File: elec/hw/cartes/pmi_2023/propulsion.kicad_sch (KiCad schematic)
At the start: 45 parts, among them Q1 SI2310, U1 DRV8231ADDAR, U2 DRV8231ADDAR, U3 EESX1321, U4 EESX1321

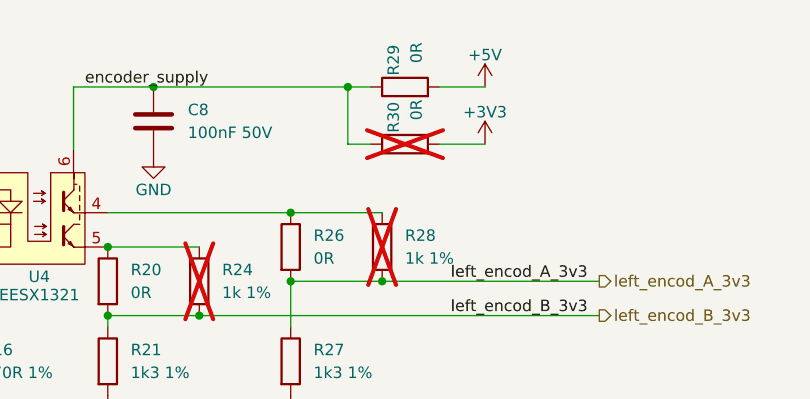
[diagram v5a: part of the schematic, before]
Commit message: modified mounting hole, replaced transistors to place them in bottom layer
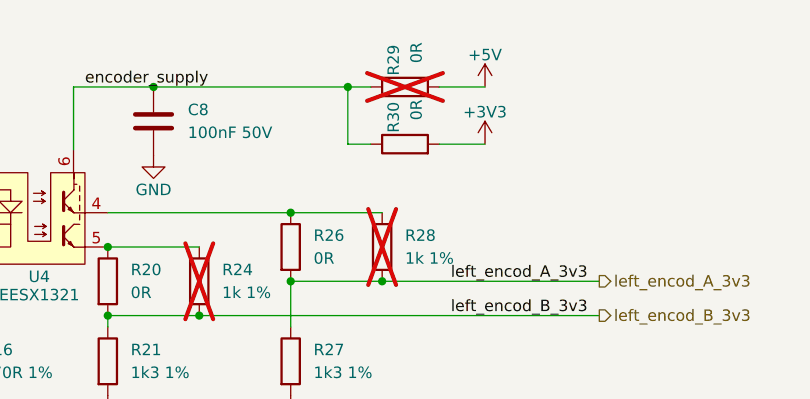
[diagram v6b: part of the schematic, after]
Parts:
- R29: now not fitted
- R30: now fitted
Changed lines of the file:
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@@
 		(in_bom yes)
 		(on_board yes)
-		(dnp yes)
+		(dnp no)
 		(property "Reference" "R30"
 			(at 207.01 35.56 0)
@@
 		(in_bom yes)
 		(on_board yes)
-		(dnp no)
+		(dnp yes)
 		(property "Reference" "R29"
 			(at 207.01 29.21 0)

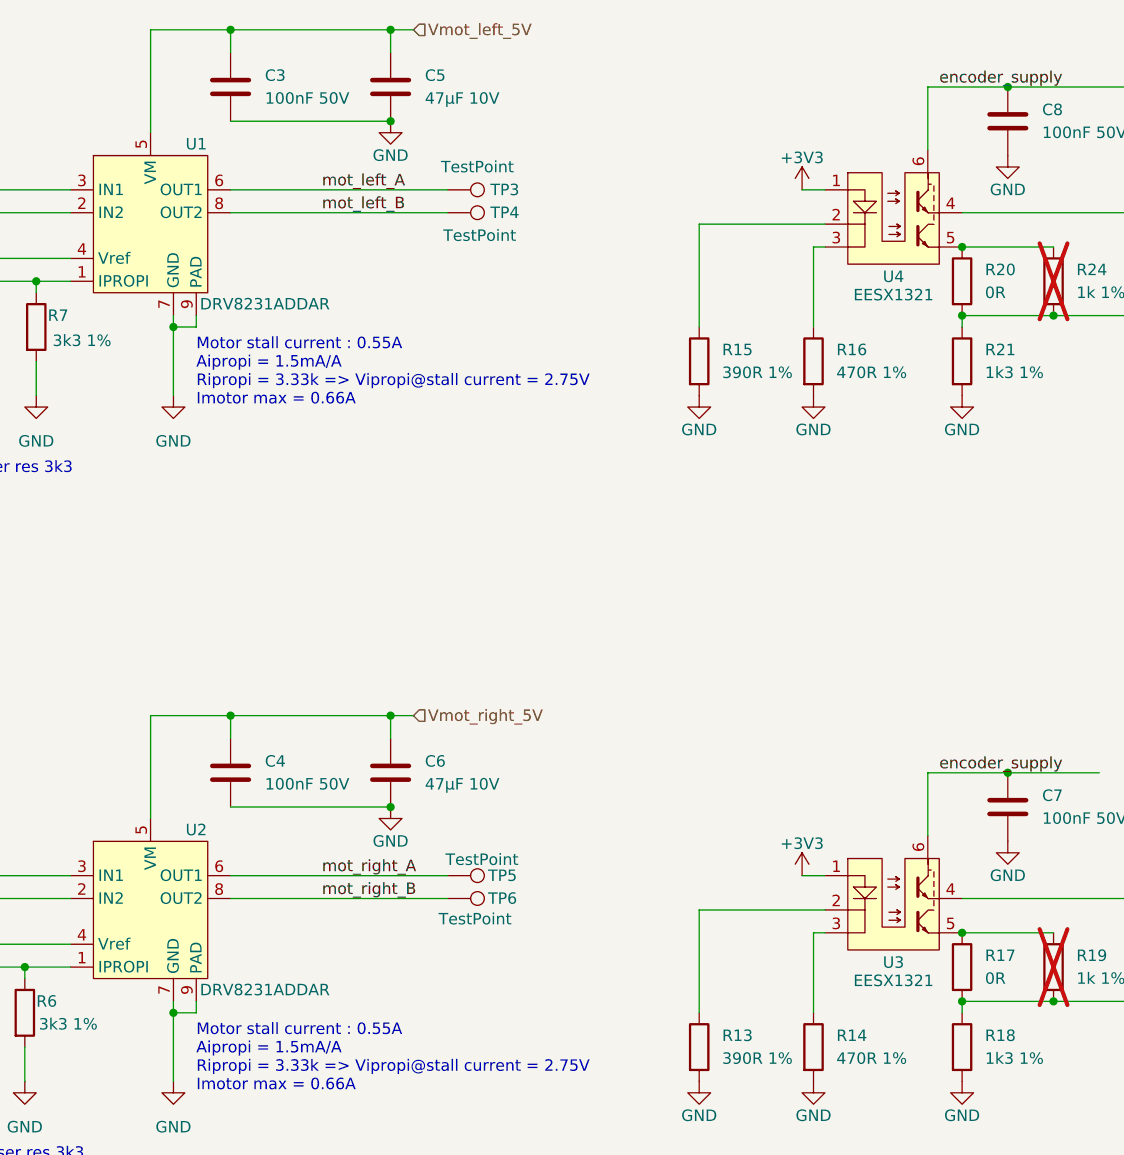
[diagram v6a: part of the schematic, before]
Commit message: XRA1200 replaced by TCA6408
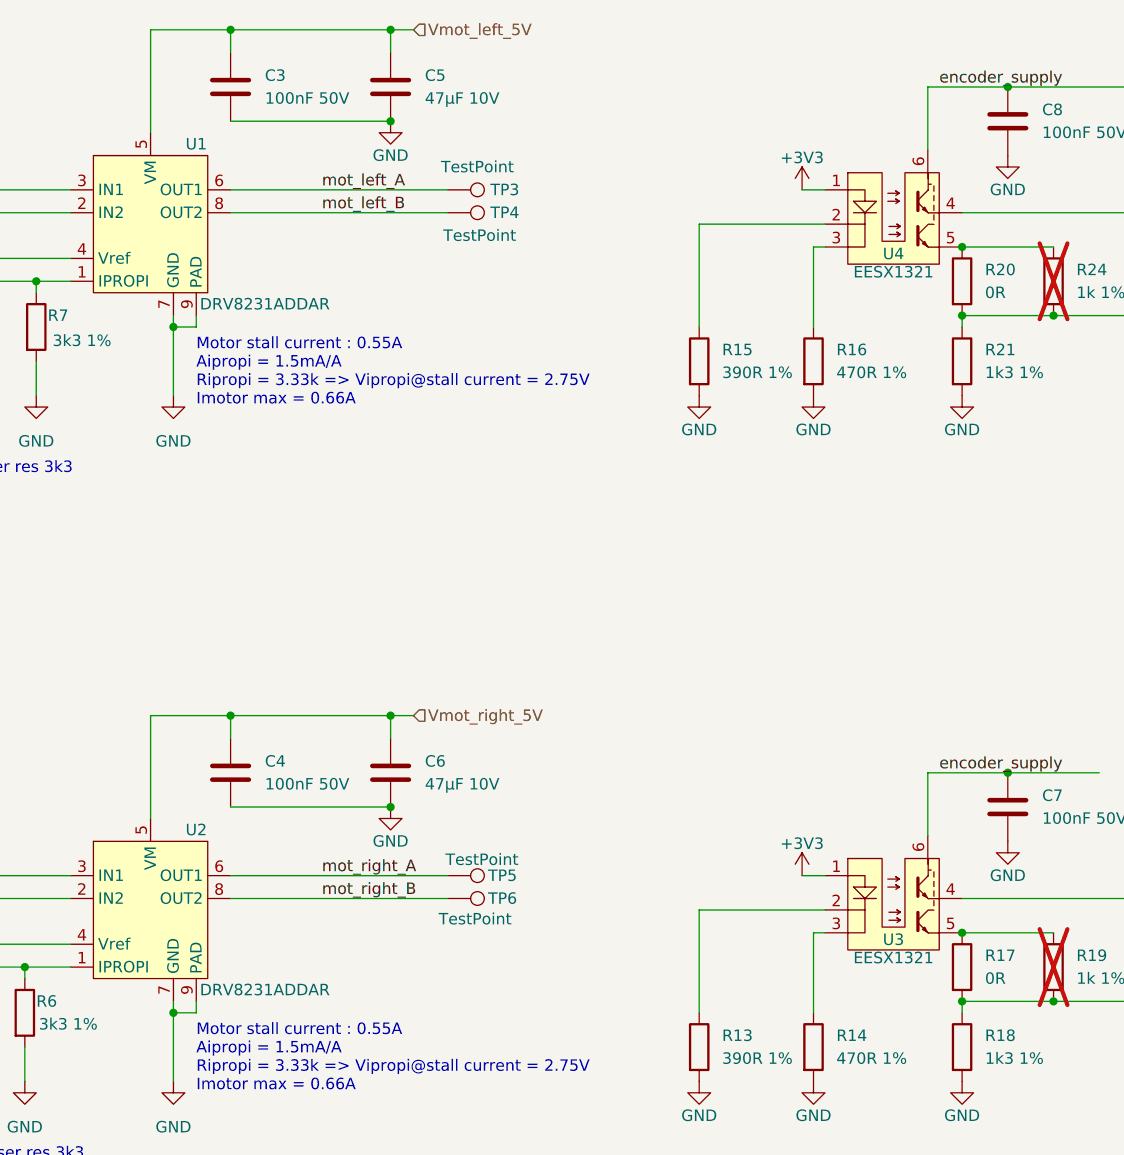
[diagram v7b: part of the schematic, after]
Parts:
- C1, C2, C3, C4, C7, C8: JLCPCB C14663 -> (none); JLCPCB Part # (none) -> C14663
- C5, C6: JLCPCB C96123 -> (none); JLCPCB Part # (none) -> C96123
- Q1: JLCPCB C2938374 -> (none); JLCPCB Part # (none) -> C2938374
- R1, R2, R3, R4, R5: JLCPCB C25803 -> (none); JLCPCB Part # (none) -> C25803
- R13, R15: JLCPCB C23151 -> (none); JLCPCB Part # (none) -> C23151
- R14, R16: JLCPCB C23179 -> (none); JLCPCB Part # (none) -> C23179
- R17, R20, R22, R26, R29, R30, R8: JLCPCB C431718 -> (none); JLCPCB Part # (none) -> C431718
- R18, R21, R23, R27: JLCPCB C22767 -> (none); JLCPCB Part # (none) -> C22767
- R19, R24, R25, R28: JLCPCB C21190 -> (none); JLCPCB Part # (none) -> C2991540
- R6, R7: JLCPCB C22978 -> (none); JLCPCB Part # (none) -> C22978
- U1, U2: JLCPCB C5218849 -> (none); JLCPCB Part # (none) -> C5218849
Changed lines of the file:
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@@
 	(paper "A4")
 	(junction
+		(at 175.26 48.26)
+		(diameter 0)
+		(color 0 0 0 0)
+	)
+	(junction
 		(at 175.26 55.88)
 		(diameter 0)
@@
 	)
 	(junction
+		(at 175.26 124.46)
+		(diameter 0)
+		(color 0 0 0 0)
+	)
+	(junction
 		(at 201.93 30.48)
 		(diameter 0)
@@
 		(color 0 0 0 0)
 	)
-	(junction
-		(at 175.26 48.26)
-		(diameter 0)
-		(color 0 0 0 0)
-	)
-	(junction
-		(at 175.26 124.46)
-		(diameter 0)
-		(color 0 0 0 0)
-	)
 	(wire
 		(pts
@@
 	(wire
 		(pts
-			(xy 160.02 48.26) (xy 158.75 48.26)
-		)
-		(stroke
-			(width 0)
-			(type default)
-		)
-	)
-	(wire
-		(pts
 			(xy 87.63 133.35) (xy 87.63 132.08)
 		)
@@
 	(wire
 		(pts
-			(xy 160.02 124.46) (xy 158.75 124.46)
+			(xy 157.48 118.11) (xy 160.02 118.11)
 		)
 		(stroke
@@
 	(wire
 		(pts
-			(xy 157.48 118.11) (xy 160.02 118.11)
+			(xy 158.75 124.46) (xy 158.75 133.35)
 		)
 		(stroke
@@
 	(wire
 		(pts
-			(xy 158.75 124.46) (xy 158.75 133.35)
+			(xy 45.72 49.53) (xy 45.72 54.61)
 		)
 		(stroke
@@
 	(wire
 		(pts
-			(xy 45.72 49.53) (xy 45.72 54.61)
+			(xy 85.09 100.33) (xy 93.98 100.33)
 		)
 		(stroke
@@
 	(wire
 		(pts
-			(xy 85.09 100.33) (xy 93.98 100.33)
+			(xy 45.72 140.97) (xy 45.72 138.43)
 		)
 		(stroke
@@
 	(wire
 		(pts
-			(xy 45.72 140.97) (xy 45.72 138.43)
+			(xy 217.17 36.83) (xy 212.09 36.83)
 		)
 		(stroke
@@
 	(wire
 		(pts
-			(xy 217.17 36.83) (xy 212.09 36.83)
+			(xy 180.34 30.48) (xy 201.93 30.48)
 		)
 		(stroke
@@
 	(wire
 		(pts
-			(xy 180.34 30.48) (xy 201.93 30.48)
+			(xy 158.75 48.26) (xy 160.02 48.26)
 		)
 		(stroke
@@
 	(wire
 		(pts
+			(xy 158.75 124.46) (xy 160.02 124.46)
+		)
+		(stroke
+			(width 0)
+			(type default)
+		)
+	)
+	(wire
+		(pts
 			(xy 45.72 64.77) (xy 45.72 62.23)
 		)
@@
 			)
 		)
-		(property "JLCPCB" "C23179"
+		(property "JLCPCB Part #" "C23179"
 			(at 158.75 137.16 0)
 			(effects
@@
 			)
 		)
-		(property "JLCPCB" "C14663"
+		(property "JLCPCB Part #" "C14663"
 			(at 45.72 58.42 0)
 			(effects
@@
 			)
 		)
-		(property "JLCPCB" "C21190"
+		(property "JLCPCB Part #" "C2991540"
 			(at 205.74 124.46 0)
 			(effects
@@
 			)
 		)
-		(property "JLCPCB" "C431718"
+		(property "JLCPCB Part #" "C431718"
 			(at 175.26 128.27 0)
 			(effects
@@
 			)
 		)
-		(property "JLCPCB" "C21190"
+		(property "JLCPCB Part #" "C2991540"
 			(at 185.42 128.27 0)
 			(effects
@@
 			)
 		)
-		(property "JLCPCB" "C25803"
+		(property "JLCPCB Part #" "C25803"
 			(at 52.07 184.15 0)
 			(effects
@@
 			)
 		)
-		(property "JLCPCB" "C431718"
+		(property "JLCPCB Part #" "C431718"
 			(at 195.58 48.26 0)
 			(effects
@@
 			)
 		)
-		(property "JLCPCB" "C14663"
+		(property "JLCPCB Part #" "C14663"
 			(at 93.98 30.48 0)
 			(effects
@@
 			)
 		)
-		(property "JLCPCB" "C2938374"
+		(property "JLCPCB Part #" "C2938374"
 			(at 83.82 177.8 0)
 			(effects
@@
 			)
 		)
-		(property "JLCPCB" "C431718"
+		(property "JLCPCB Part #" "C431718"
 			(at 175.26 52.07 0)
 			(effects
@@
 			)
 		)
-		(property "JLCPCB" "C25803"
+		(property "JLCPCB Part #" "C25803"
 			(at 26.67 132.08 0)
 			(effects
@@
 			)
 		)
-		(property "JLCPCB" "C431718"
+		(property "JLCPCB Part #" "C431718"
 			(at 80.01 166.37 0)
 			(effects
@@
 			)
 		)
-		(property "JLCPCB" "C5218849"
+		(property "JLCPCB Part #" "C5218849"
 			(at 85.09 46.99 0)
 			(effects
@@
 			)
 		)
-		(property "JLCPCB" "C14663"
+		(property "JLCPCB Part #" "C14663"
 			(at 45.72 134.62 0)
 			(effects
@@
 			)
 		)
-		(property "JLCPCB" "C21190"
+		(property "JLCPCB Part #" "C2991540"
 			(at 185.42 52.07 0)
 			(effects
@@
 	(symbol
 		(lib_id "cocotter_ic:EESX1321")
-		(at 167.64 121.92 0)
+		(at 167.64 119.38 0)
 		(unit 1)
 		(exclude_from_sim no)
@@
 		(dnp no)
 		(property "Reference" "U3"
-			(at 167.64 127.762 0)
+			(at 167.64 125.222 0)
 			(effects
 				(font
@@
 		)
 		(property "Value" "EESX1321"
-			(at 167.64 129.794 0)
+			(at 167.64 127.254 0)
 			(effects
 				(font
@@
 		)
 		(property "Footprint" "cocotter_ic:EESX1321"
-			(at 176.53 116.84 0)
+			(at 176.53 114.3 0)
 			(effects
 				(font
@@
 		)
 		(property "Datasheet" ""
-			(at 176.53 116.84 0)
+			(at 176.53 114.3 0)
 			(effects
 				(font
@@
 		)
 		(property "Description" ""
-			(at 167.64 121.92 0)
+			(at 167.64 119.38 0)
 			(effects
 				(font
@@
 			)
 		)
-		(property "JLCPCB" "C22767"
+		(property "JLCPCB Part #" "C22767"
 			(at 195.58 60.96 0)
 			(effects
@@
 			)
 		)
-		(property "JLCPCB" "C22767"
+		(property "JLCPCB Part #" "C22767"
 			(at 195.58 137.16 0)
 			(effects
@@
 			)
 		)
-		(property "JLCPCB" "C96123"
+		(property "JLCPCB Part #" "C96123"
 			(at 111.76 30.48 0)
 			(effects
@@
 			)
 		)
-		(property "JLCPCB" "C25803"
+		(property "JLCPCB Part #" "C25803"
 			(at 35.56 132.08 0)
 			(effects
@@
 			)
 		)
-		(property "JLCPCB" "C21190"
+		(property "JLCPCB Part #" "C2991540"
 			(at 205.74 48.26 0)
 			(effects
@@
 			)
 		)
-		(property "JLCPCB" "C5218849"
+		(property "JLCPCB Part #" "C5218849"
 			(at 85.09 123.19 0)
 			(effects
@@
 			)
 		)
-		(property "JLCPCB" "C431718"
+		(property "JLCPCB Part #" "C431718"
 			(at 208.28 36.83 0)
 			(effects
@@
 			)
 		)
-		(property "JLCPCB" "C14663"
+		(property "JLCPCB Part #" "C14663"
 			(at 180.34 34.29 0)
 			(effects
@@
 	(symbol
 		(lib_id "cocotter_ic:EESX1321")
-		(at 167.64 45.72 0)
+		(at 167.64 43.18 0)
 		(unit 1)
 		(exclude_from_sim no)
@@
 		(dnp no)
 		(property "Reference" "U4"
-			(at 167.64 51.562 0)
+			(at 167.64 49.022 0)
 			(effects
 				(font
@@
 		)
 		(property "Value" "EESX1321"
-			(at 167.64 53.594 0)
+			(at 167.64 51.054 0)
 			(effects
 				(font
@@
 		)
 		(property "Footprint" "cocotter_ic:EESX1321"
-			(at 176.53 40.64 0)
+			(at 176.53 38.1 0)
 			(effects
 				(font
@@
 		)
 		(property "Datasheet" ""
-			(at 176.53 40.64 0)
+			(at 176.53 38.1 0)
 			(effects
 				(font
@@
 		)
 		(property "Description" ""
-			(at 167.64 45.72 0)
+			(at 167.64 43.18 0)
 			(effects
 				(font
@@
 			)
 		)
-		(property "JLCPCB" "C22978"
+		(property "JLCPCB Part #" "C22978"
 			(at 71.12 133.35 0)
 			(effects
@@
 			)
 		)
-		(property "JLCPCB" "C23151"
+		(property "JLCPCB Part #" "C23151"
 			(at 146.05 137.16 0)
 			(effects
@@
 			)
 		)
-		(property "JLCPCB" "C431718"
+		(property "JLCPCB Part #" "C431718"
 			(at 195.58 124.46 0)
 			(effects
@@
 			)
 		)
-		(property "JLCPCB" "C14663"
+		(property "JLCPCB Part #" "C14663"
 			(at 180.34 110.49 0)
 			(effects
@@
 			)
 		)
-		(property "JLCPCB" "C23179"
+		(property "JLCPCB Part #" "C23179"
 			(at 158.75 60.96 0)
 			(effects
@@
 			)
 		)
-		(property "JLCPCB" "C96123"
+		(property "JLCPCB Part #" "C96123"
 			(at 111.76 106.68 0)
 			(effects
@@
 			)
 		)
-		(property "JLCPCB" "C14663"
+		(property "JLCPCB Part #" "C14663"
 			(at 93.98 106.68 0)
 			(effects
@@
 			)
 		)
-		(property "JLCPCB" "C25803"
+		(property "JLCPCB Part #" "C25803"
 			(at 26.67 55.88 0)
 			(effects
@@
 			)
 		)
-		(property "JLCPCB" "C22767"
+		(property "JLCPCB Part #" "C22767"
 			(at 175.26 137.16 0)
 			(effects
@@
 			)
 		)
-		(property "JLCPCB" "C22767"
+		(property "JLCPCB Part #" "C22767"
 			(at 175.26 60.96 0)
 			(effects
@@
 			)
 		)
-		(property "JLCPCB" "C22978"
+		(property "JLCPCB Part #" "C22978"
 			(at 72.39 57.15 0)
 			(effects
@@
 			)
 		)
-		(property "JLCPCB" "C23151"
+		(property "JLCPCB Part #" "C23151"
 			(at 146.05 60.96 0)
 			(effects
@@
 			)
 		)
-		(property "JLCPCB" "C25803"
+		(property "JLCPCB Part #" "C25803"
 			(at 35.56 55.88 0)
 			(effects
@@
 			)
 		)
-		(property "JLCPCB" "C431718"
+		(property "JLCPCB Part #" "C431718"
 			(at 208.28 30.48 0)
 			(effects

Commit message: bom updated and component selection optimized to decrease bom cost
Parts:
- R1, R2, R3, R4, R5: value 100k -> 91k 1%; symbol cocotter_resistors:R_100k_0603_1% -> cocotter_resistors:R_91k_0603_1%; JLCPCB Part # C25803 -> C23265; Specification 100k 0603 1% 100mW -> 91k 0603 1% 100mW; mouser 603-RC0603FR-10100KL -> (none)
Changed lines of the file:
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@@
 	)
 	(symbol
-		(lib_id "cocotter_resistors:R_100k_0603_1%")
+		(lib_id "cocotter_resistors:R_91k_0603_1%")
 		(at 52.07 184.15 0)
 		(unit 1)
@@
 			)
 		)
-		(property "Value" "100k"
+		(property "Value" "91k 1%"
 			(at 54.61 185.4199 0)
 			(effects
@@
 			)
 		)
-		(property "Specification" "100k 0603 1% 100mW"
+		(property "Specification" "91k 0603 1% 100mW"
 			(at 52.07 184.15 0)
 			(effects
@@
 			)
 		)
-		(property "mouser" "603-RC0603FR-10100KL"
+		(property "mouser" ""
 			(at 52.07 184.15 0)
 			(effects
@@
 			)
 		)
-		(property "JLCPCB Part #" "C25803"
+		(property "JLCPCB Part #" "C23265"
 			(at 52.07 184.15 0)
 			(effects
@@
 	)
 	(symbol
-		(lib_id "cocotter_resistors:R_100k_0603_1%")
+		(lib_id "cocotter_resistors:R_91k_0603_1%")
 		(at 26.67 132.08 0)
 		(unit 1)
@@
 			)
 		)
-		(property "Value" "100k"
+		(property "Value" "91k 1%"
 			(at 29.21 133.3499 0)
 			(effects
@@
 			)
 		)
-		(property "Specification" "100k 0603 1% 100mW"
+		(property "Specification" "91k 0603 1% 100mW"
 			(at 26.67 132.08 0)
 			(effects
@@
 			)
 		)
-		(property "mouser" "603-RC0603FR-10100KL"
+		(property "mouser" ""
 			(at 26.67 132.08 0)
 			(effects
@@
 			)
 		)
-		(property "JLCPCB Part #" "C25803"
+		(property "JLCPCB Part #" "C23265"
 			(at 26.67 132.08 0)
 			(effects
@@
 	)
 	(symbol
-		(lib_id "cocotter_resistors:R_100k_0603_1%")
+		(lib_id "cocotter_resistors:R_91k_0603_1%")
 		(at 35.56 132.08 0)
 		(unit 1)
@@
 			)
 		)
-		(property "Value" "100k"
+		(property "Value" "91k 1%"
 			(at 38.1 133.3499 0)
 			(effects
@@
 			)
 		)
-		(property "Specification" "100k 0603 1% 100mW"
+		(property "Specification" "91k 0603 1% 100mW"
 			(at 35.56 132.08 0)
 			(effects
@@
 			)
 		)
-		(property "mouser" "603-RC0603FR-10100KL"
+		(property "mouser" ""
 			(at 35.56 132.08 0)
 			(effects
@@
 			)
 		)
-		(property "JLCPCB Part #" "C25803"
+		(property "JLCPCB Part #" "C23265"
 			(at 35.56 132.08 0)
 			(effects
@@
 	)
 	(symbol
-		(lib_id "cocotter_resistors:R_100k_0603_1%")
+		(lib_id "cocotter_resistors:R_91k_0603_1%")
 		(at 26.67 55.88 0)
 		(unit 1)
@@
 			)
 		)
-		(property "Value" "100k"
+		(property "Value" "91k 1%"
 			(at 29.21 57.1499 0)
 			(effects
@@
 			)
 		)
-		(property "Specification" "100k 0603 1% 100mW"
+		(property "Specification" "91k 0603 1% 100mW"
 			(at 26.67 55.88 0)
 			(effects
@@
 			)
 		)
-		(property "mouser" "603-RC0603FR-10100KL"
+		(property "mouser" ""
 			(at 26.67 55.88 0)
 			(effects
@@
 			)
 		)
-		(property "JLCPCB Part #" "C25803"
+		(property "JLCPCB Part #" "C23265"
 			(at 26.67 55.88 0)
 			(effects
@@
 	)
 	(symbol
-		(lib_id "cocotter_resistors:R_100k_0603_1%")
+		(lib_id "cocotter_resistors:R_91k_0603_1%")
 		(at 35.56 55.88 0)
 		(unit 1)
@@
 			)
 		)
-		(property "Value" "100k"
+		(property "Value" "91k 1%"
 			(at 38.1 57.1499 0)
 			(effects
@@
 			)
 		)
-		(property "Specification" "100k 0603 1% 100mW"
+		(property "Specification" "91k 0603 1% 100mW"
 			(at 35.56 55.88 0)
 			(effects
@@
 			)
 		)
-		(property "mouser" "603-RC0603FR-10100KL"
+		(property "mouser" ""
 			(at 35.56 55.88 0)
 			(effects
@@
 			)
 		)
-		(property "JLCPCB Part #" "C25803"
+		(property "JLCPCB Part #" "C23265"
 			(at 35.56 55.88 0)
 			(effects
